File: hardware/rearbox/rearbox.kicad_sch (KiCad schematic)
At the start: 21 parts, among them J1 Goldpin, J2 STDC14, SW1 Reset, U1 LM4040C33FTA, U2 STM32G473RCTx, Y1 48MHz

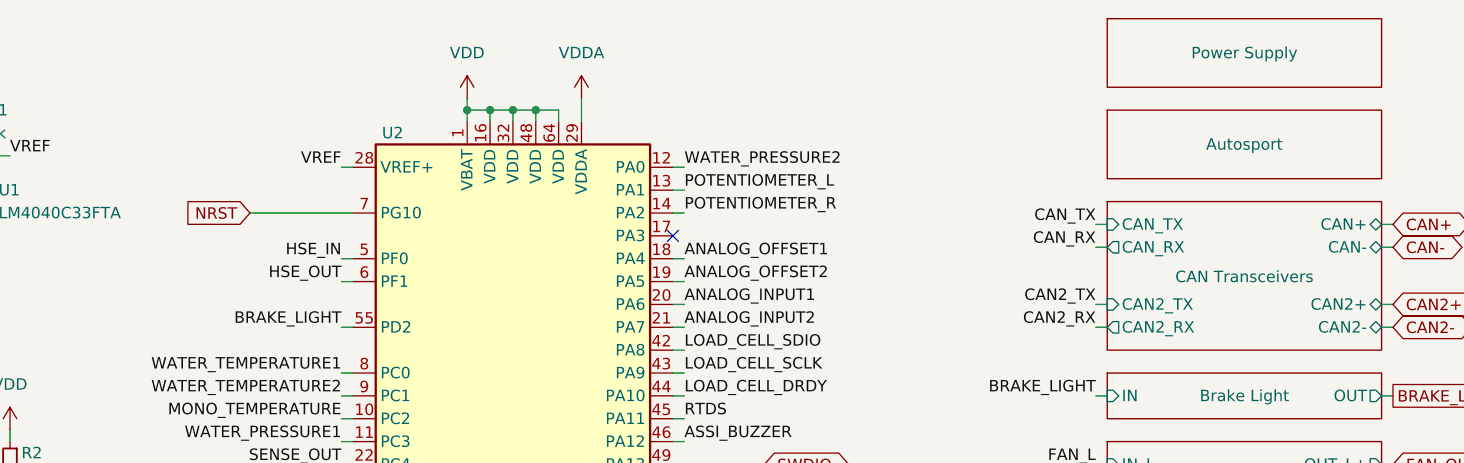
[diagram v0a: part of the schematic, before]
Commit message: Add the connector board
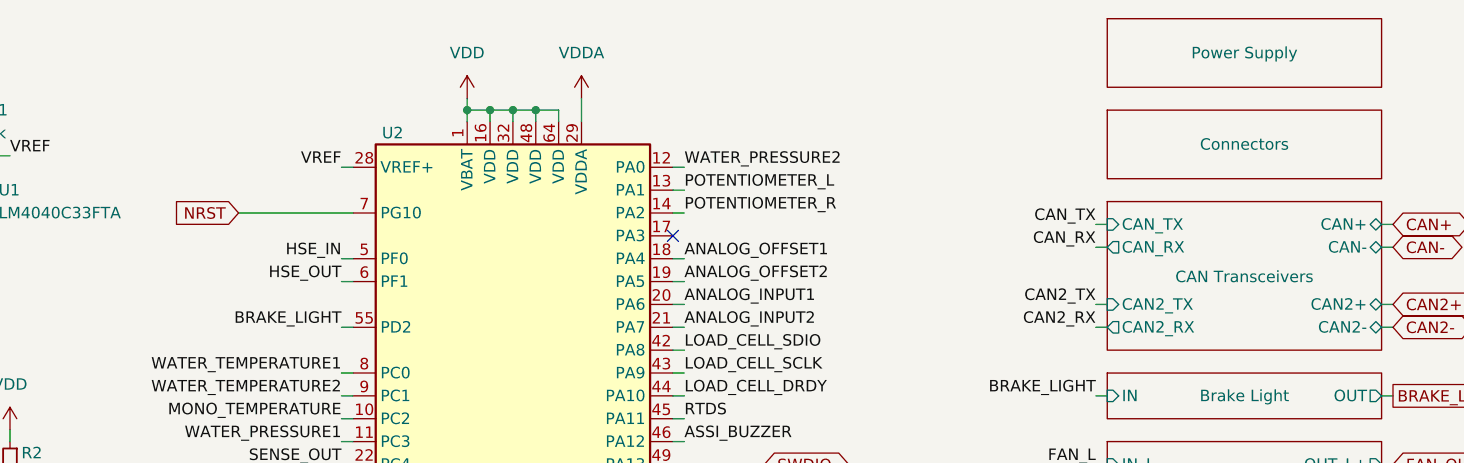
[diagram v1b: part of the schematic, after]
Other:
- sheet Autosport renamed Connectors
- sheet Connectors: file autosport.kicad_sch -> connectors.kicad_sch
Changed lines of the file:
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@@
     (stroke (width 0) (type default))
   )
-  (wire (pts (xy 54.61 41.91) (xy 66.04 41.91))
+  (wire (pts (xy 53.34 41.91) (xy 66.04 41.91))
     (stroke (width 0) (type default))
   )
@@
     )
   )
-  (global_label "NRST" (shape input) (at 54.61 41.91 180) (fields_autoplaced)
+  (global_label "NRST" (shape input) (at 53.34 41.91 180) (fields_autoplaced)
     (effects (font (size 1.27 1.27)) (justify right))
-    (property "Intersheetrefs" "${INTERSHEET_REFS}" (at 46.9266 41.91 0)
+    (property "Intersheetrefs" "${INTERSHEET_REFS}" (at 45.6566 41.91 0)
       (effects (font (size 1.27 1.27)) (justify right) hide)
     )
@@
     (stroke (width 0.1524) (type solid))
     (fill (color 0 0 0 0.0000))
-    (property "Sheetname" "Autosport" (at 165.1 34.29 0)
-      (effects (font (size 1.27 1.27)))
-    )
-    (property "Sheetfile" "autosport.kicad_sch" (at 149.86 50.1146 0)
+    (property "Sheetname" "Connectors" (at 165.1 34.29 0)
+      (effects (font (size 1.27 1.27)))
+    )
+    (property "Sheetfile" "connectors.kicad_sch" (at 149.86 50.1146 0)
       (effects (font (size 1.27 1.27)) (justify left top) hide)
     )

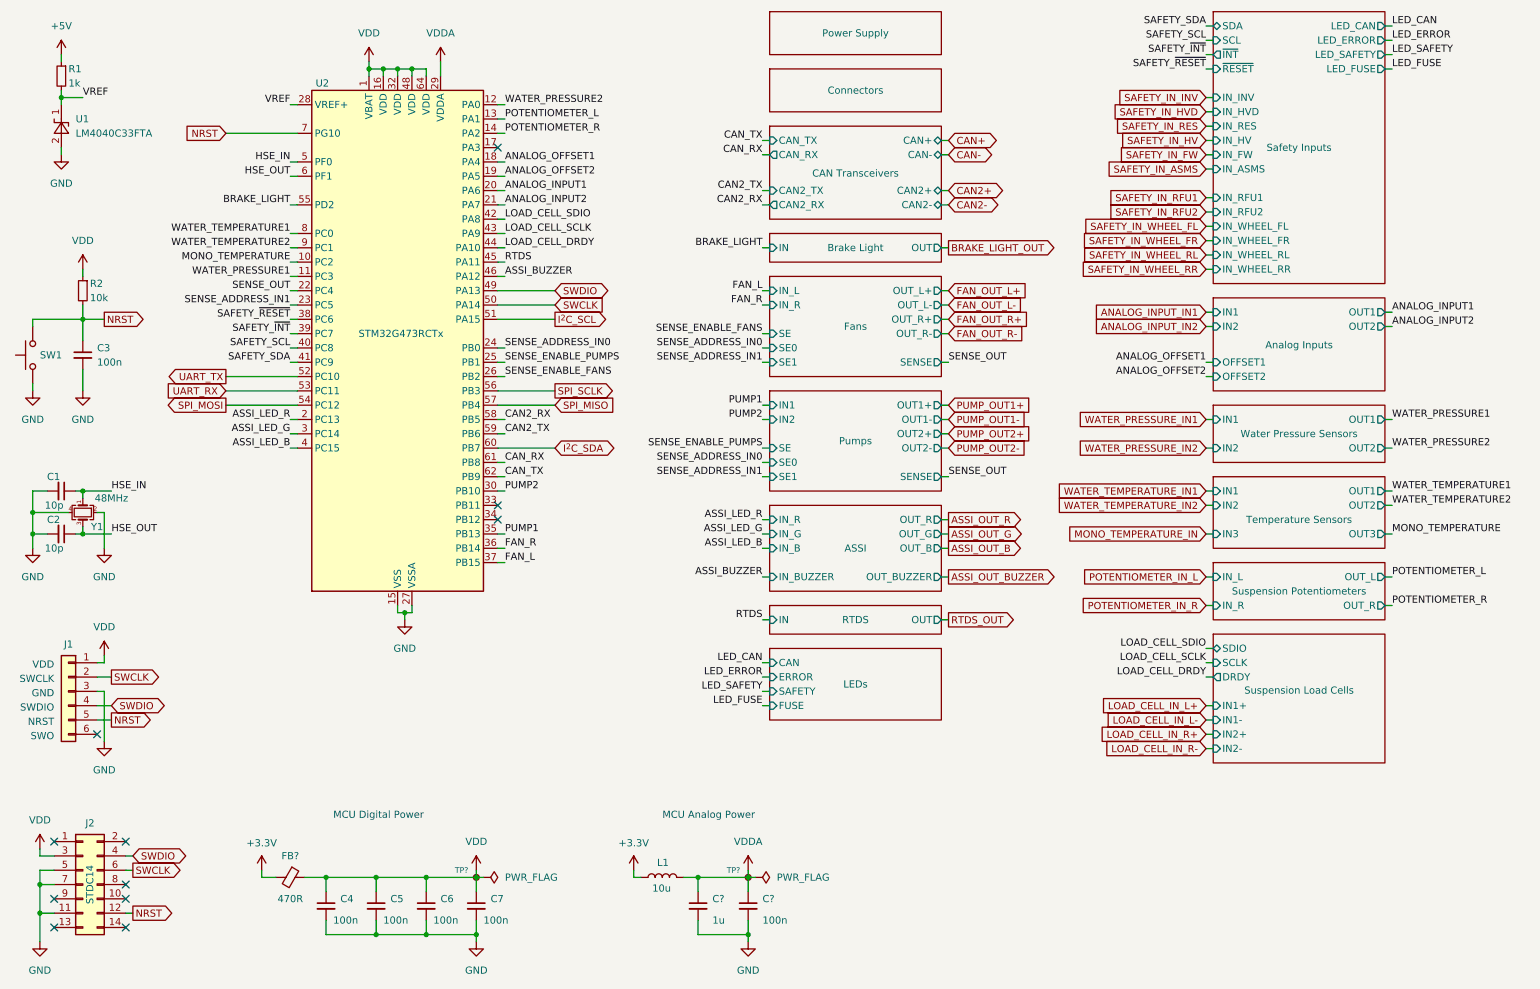
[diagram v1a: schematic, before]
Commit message: Place components on the PCB
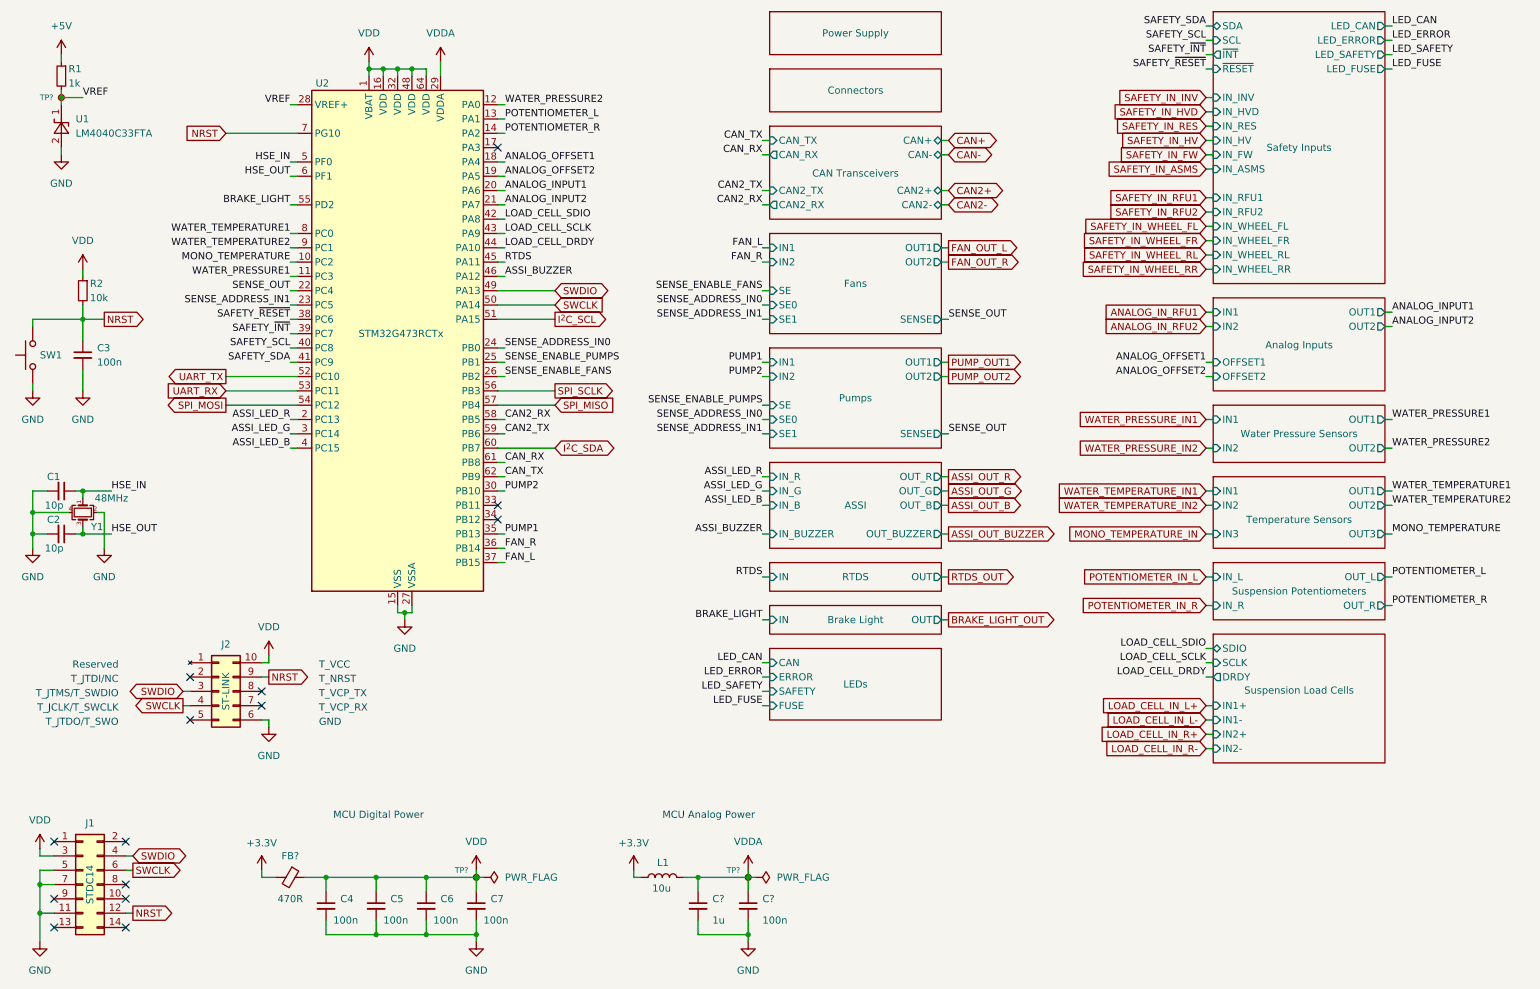
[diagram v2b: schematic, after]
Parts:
- removed J1: Goldpin, Connector_PinHeader_2.54mm:PinHeader_1x06_P2.54mm_Vertical, symbol Connector_Generic:Conn_01x06
- added J2: ST-LINK, Local_Library:STLINK-V3MINIE, symbol STLINK-V3MINIE:STLINK-V3MINIE
- added TP?: TestPoint_Small, TestPoint:TestPoint_Pad_D1.0mm, symbol Connector:TestPoint_Small
- U1: symbol Reference_Voltage:LM4040DBZ-3 -> LM4040:LM4040
- renumbered J2 to J1
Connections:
- net GND: now also J2.6 (GND)
- net NRST: now also J2.9 (T_NRST)
- net SWCLK: now also J2.4 (T_JCLK/T_SWCLK)
- net SWDIO: now also J2.3 (T_JTMS/T_SWDIO)
- net VDD: now also J2.10 (T_VCC)
- net VREF: now also TP?.1
- no-connect marks 11 -> 14
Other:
- sheet Fans: file fans.kicad_sch -> fused_output.kicad_sch
- sheet Fans ports: added IN1, IN2, OUT1, OUT2; removed IN_L, IN_R, OUT_L+, OUT_L-, OUT_R+, OUT_R-
- sheet Pumps: file pumps.kicad_sch -> fused_output.kicad_sch
- sheet Pumps ports: added OUT1, OUT2; removed OUT1+, OUT1-, OUT2+, OUT2-
- note added: "Reserved"
- note added: "T_JCLK/T_SWCLK"
- note added: "T_JTDI/NC"
- note added: "T_JTDO/T_SWO"
- note added: "T_JTMS/T_SWDIO"
- note added: "T_NRST"
- note added: "T_VCC"
- note added: "T_VCP_RX"
- note added: "T_VCP_TX"
- note removed: "NRST"
- note removed: "SWCLK"
- note removed: "SWDIO"
- note removed: "SWO"
- note removed: "VDD"

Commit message: Align footprint references
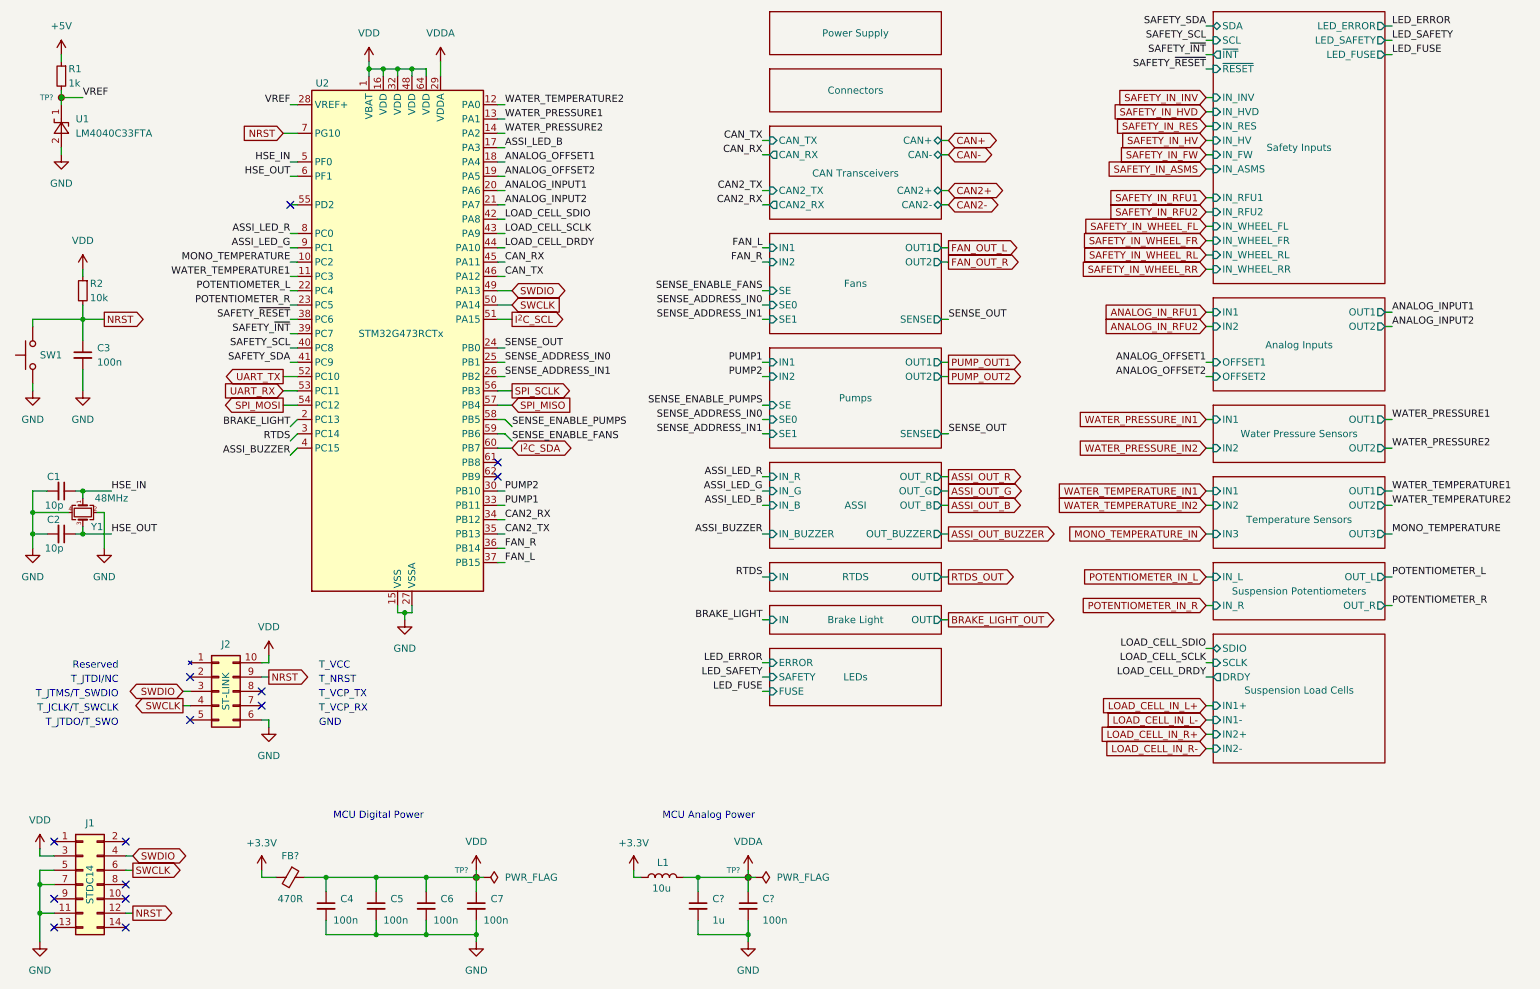
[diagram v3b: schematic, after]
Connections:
- net ASSI_BUZZER: now also U2.4 (PC15); no longer U2.46 (PA12)
- net ASSI_LED_B: now also U2.17 (PA3); no longer U2.4 (PC15)
- net ASSI_LED_G: now also U2.9 (PC1); no longer U2.3 (PC14)
- net ASSI_LED_R: now also U2.8 (PC0); no longer U2.2 (PC13)
- net BRAKE_LIGHT: now also U2.2 (PC13); no longer U2.55 (PD2)
- net CAN2_RX: now also U2.34 (PB12); no longer U2.58 (PB5)
- net CAN2_TX: now also U2.35 (PB13); no longer U2.59 (PB6)
- net CAN_RX: now also U2.45 (PA11); no longer U2.61 (PB8)
- net CAN_TX: now also U2.46 (PA12); no longer U2.62 (PB9)
- net POTENTIOMETER_L: now also U2.22 (PC4); no longer U2.13 (PA1)
- net POTENTIOMETER_R: now also U2.23 (PC5); no longer U2.14 (PA2)
- net PUMP1: now also U2.33 (PB11); no longer U2.35 (PB13)
- net RTDS: now also U2.3 (PC14); no longer U2.45 (PA11)
- net SENSE_ADDRESS_IN0: now also U2.25 (PB1); no longer U2.24 (PB0)
- net SENSE_ADDRESS_IN1: now also U2.26 (PB2); no longer U2.23 (PC5)
- net SENSE_ENABLE_FANS: now also U2.59 (PB6); no longer U2.26 (PB2)
- net SENSE_ENABLE_PUMPS: now also U2.58 (PB5); no longer U2.25 (PB1)
- net SENSE_OUT: now also U2.24 (PB0); no longer U2.22 (PC4)
- net WATER_PRESSURE1: now also U2.13 (PA1); no longer U2.11 (PC3)
- net WATER_PRESSURE2: now also U2.14 (PA2); no longer U2.12 (PA0)
- net WATER_TEMPERATURE1: now also U2.11 (PC3); no longer U2.8 (PC0)
- net WATER_TEMPERATURE2: now also U2.12 (PA0); no longer U2.9 (PC1)
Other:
- sheet LEDs ports: added none; removed CAN
- sheet Safety Inputs ports: added none; removed LED_CAN
